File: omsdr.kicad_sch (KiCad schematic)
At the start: 54 parts, among them J1 I/Q Out, J2 ANT, J3 ISP, J4 LO, J5 I/Q Out, J8 PWR, SW1 SW_SPST, SW2 SW_SPST, T1 CX2074NL, U1 LT6231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

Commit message: Adding year 2022 to copyright info
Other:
- note added: "Design by Matt Weyland (HB9FRV) Based on work by Tony Parks (c) 2017,18,19,22 CC-BY-SA"
- note removed: "Design by Matt Weyland (HB9FRV) Based on work by Tony Parks (c) 2017,18,19, CC-BY-SA"
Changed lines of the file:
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@@
     (effects (font (size 5.0038 5.0038) (thickness 1.0008) bold) (justify left bottom))
   )
-  (text "Design by Matt Weyland (HB9FRV)\n\nBased on work by Tony Parks\n(c) 2017,18,19, CC-BY-SA"
+  (text "Design by Matt Weyland (HB9FRV)\n\nBased on work by Tony Parks\n(c) 2017,18,19,22 CC-BY-SA"
     (at 204.47 158.75 0)
     (effects (font (size 2.9972 2.9972)) (justify left bottom))

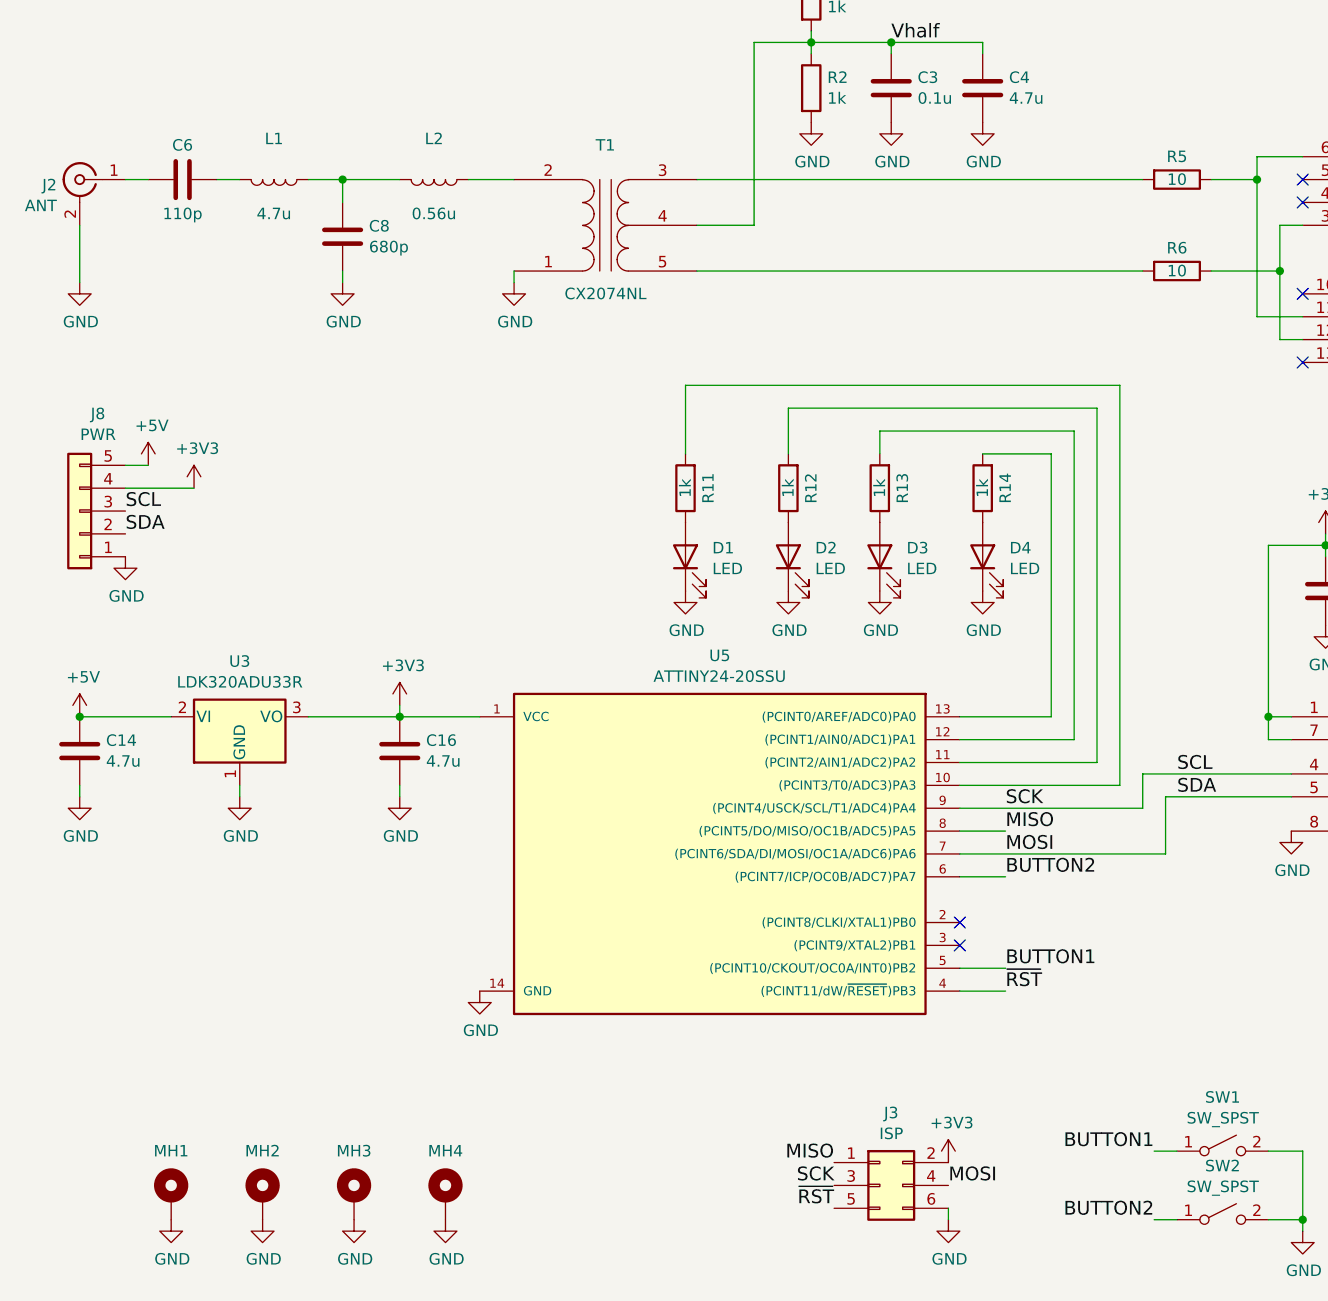
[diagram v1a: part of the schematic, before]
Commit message: Using attiny24 from the KiCad library (sch & pcb)
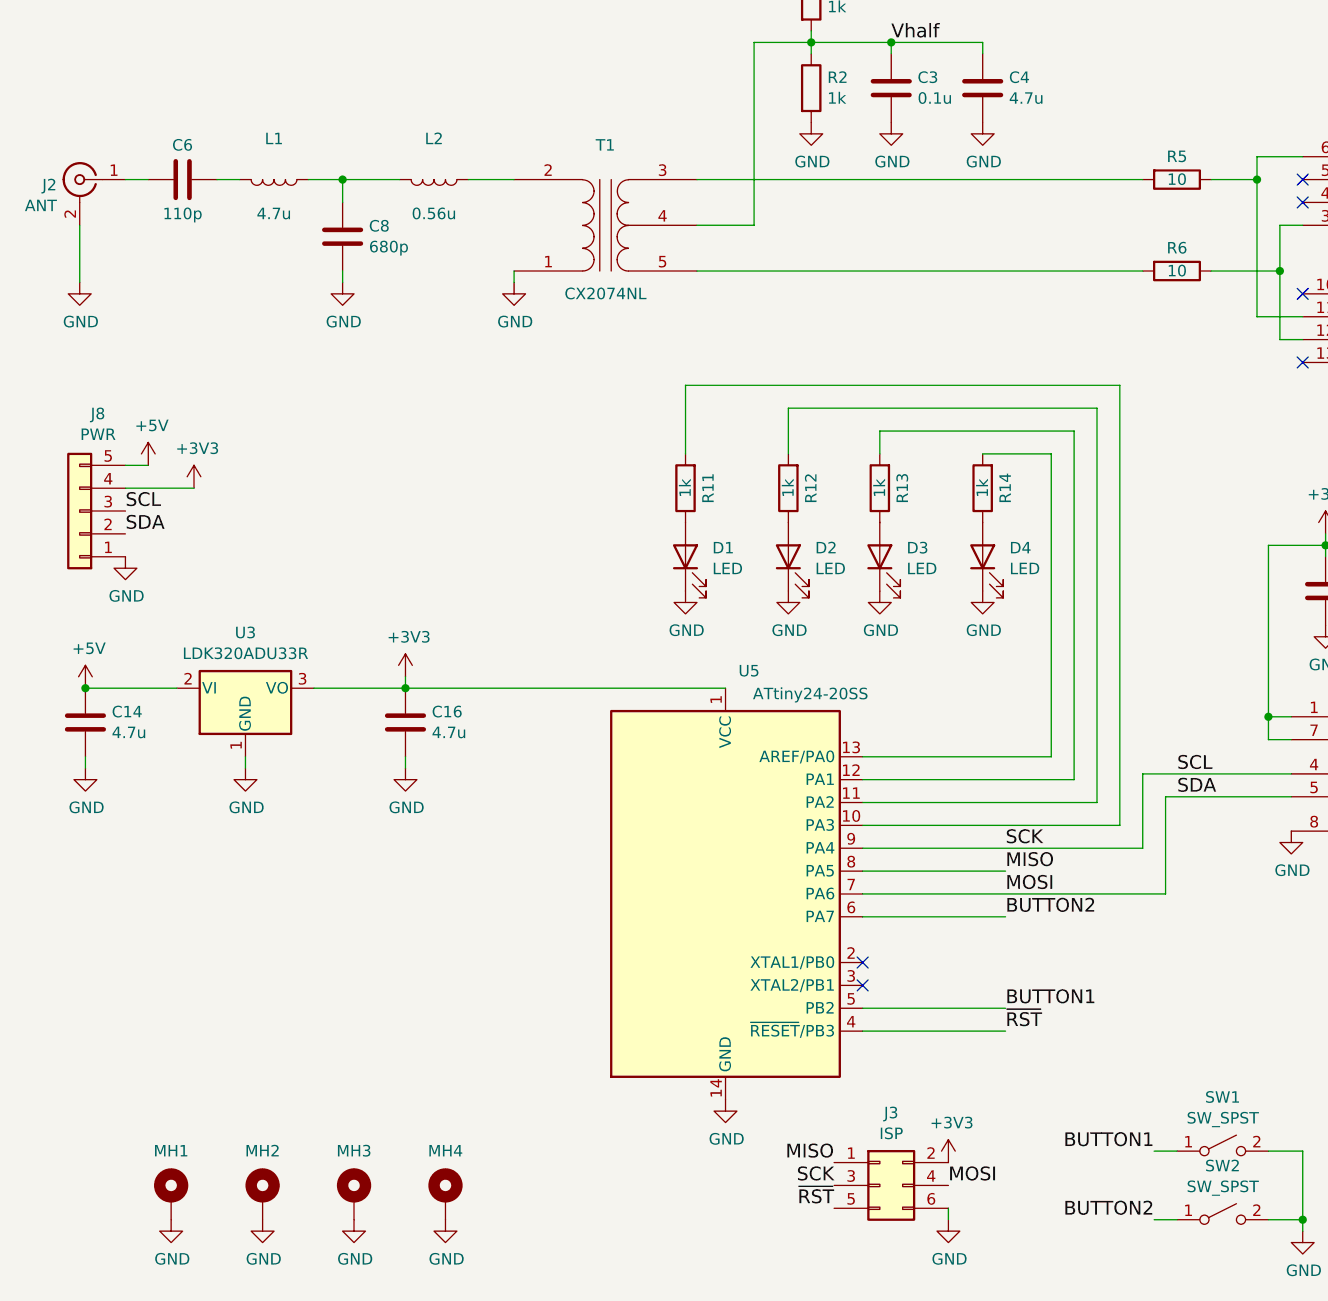
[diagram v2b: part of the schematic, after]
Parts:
- removed U5: ATTINY24-20SSU, IPC7351-Most:SOIC127P600X175-14, symbol omsdr-rescue:ATTINY24-20SSU-atmel
- added U5: ATtiny24-20SS, Package_SO:SOIC-14_3.9x8.7mm_P1.27mm, symbol MCU_Microchip_ATtiny:ATtiny24-20SS
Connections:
- net +3V3: now also U5.1 (VCC)
- net BUTTON1: now also U5.5 (PB2)
- net BUTTON2: now also U5.6 (PA7)
- net GND: now also U5.14 (GND)
- net MISO: now also U5.8 (PA5)
- net MOSI: now also U5.7 (PA6)
- net SCK: now also U5.9 (PA4)
- net ~{RST}: now also U5.4 (~{RESET}/PB3)
- net at R11.2: now also U5.10 (PA3)
- net at R12.2: now also U5.11 (PA2)
- net at R13.2: now also U5.12 (PA1)
- net at R14.2: now also U5.13 (AREF/PA0)
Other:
- moved on the sheet: C14, C16, U3

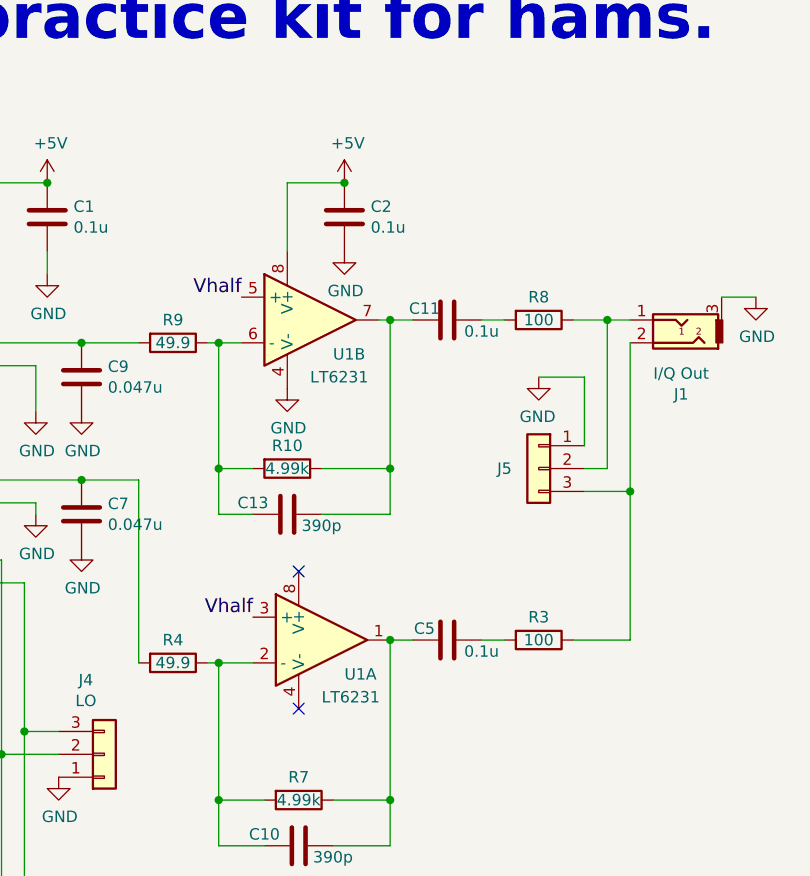
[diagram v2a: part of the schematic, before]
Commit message: Using LC6231 from the KiCad library (sch & pcb)
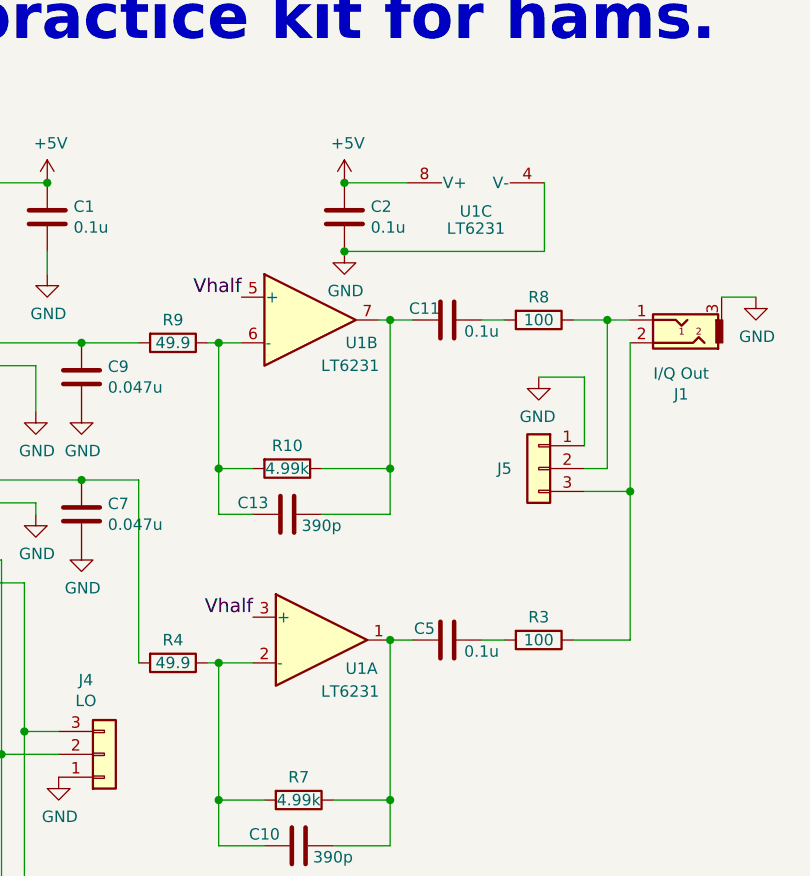
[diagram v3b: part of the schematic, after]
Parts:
- removed U1: LT6231, IPC7351-Most:SOIC127P600X175-8, symbol omsdr-rescue:LT6233-linear
- added U1: LT6231, Package_SO:SO-8_3.9x4.9mm_P1.27mm, symbol Amplifier_Operational:LT6234
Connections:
- net +5V: now also U1.8 (V+)
- net GND: now also U1.4 (V-)
- net Vhalf: now also U1.3 (+), U1.5 (+)
- net at C10.2, C5.1, R7.1: now also U1.1
- net at C10.1, R4.1, R7.2: now also U1.2 (-)
- net at C13.1, R10.2, R9.1: now also U1.6 (-)
- net at C11.1, C13.2, R10.1: now also U1.7
- no-connect marks 9 -> 7

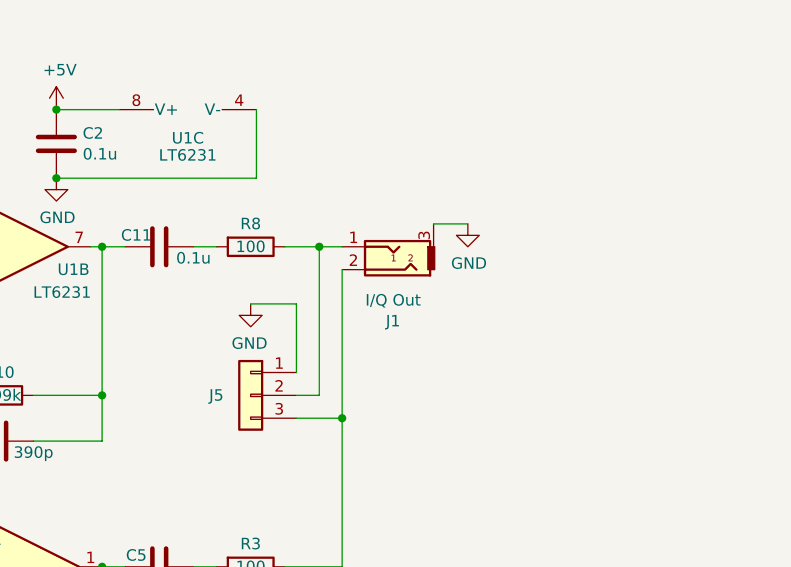
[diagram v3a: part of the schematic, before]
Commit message: Using headphone connector from the KiCad library (sch & pcb)
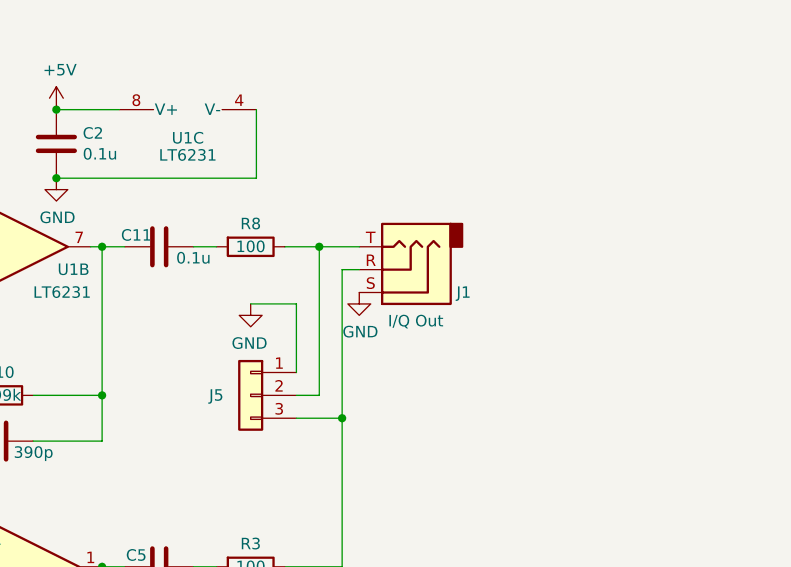
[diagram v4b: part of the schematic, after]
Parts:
- removed J1: I/Q Out, conn-cui:CONN-SJ-3523-SMT, symbol omsdr-rescue:Audio-Jack-3-Connector
- added J1: I/Q Out, Connector_Audio:Jack_3.5mm_CUI_SJ-3523-SMT_Horizontal, symbol Connector:AudioJack3
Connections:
- net GND: now also J1.S
- net at J5.2 (Pin_2), R8.1: now also J1.T
- net at J5.3 (Pin_3), R3.1: now also J1.R
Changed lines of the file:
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@@
     (stroke (width 0) (type default) (color 0 0 0 0))
   )
-  (wire (pts (xy 261.62 57.15) (xy 264.16 57.15))
+  (wire (pts (xy 261.62 57.15) (xy 266.065 57.15))
     (stroke (width 0) (type default) (color 0 0 0 0))
   )
@@
     (stroke (width 0) (type default) (color 0 0 0 0))
   )
-  (wire (pts (xy 274.32 54.61) (xy 278.13 54.61))
-    (stroke (width 0) (type default) (color 0 0 0 0))
-  )
   (wire (pts (xy 157.48 170.18) (xy 161.29 170.18))
     (stroke (width 0) (type default) (color 0 0 0 0))
@@
   )
   (wire (pts (xy 222.25 73.66) (xy 218.44 73.66))
+    (stroke (width 0) (type default) (color 0 0 0 0))
+  )
+  (wire (pts (xy 264.16 59.69) (xy 266.065 59.69))
     (stroke (width 0) (type default) (color 0 0 0 0))
   )
@@
     (pin "2")
   )
-  (symbol (lib_id "omsdr-rescue:Audio-Jack-3-Connector") (at 269.24 57.15 180) (unit 1)
-    (in_bom yes) (on_board yes)
-    (property "Reference" "J1" (id 0) (at 269.8242 65.405 0))
-    (property "Value" "I/Q Out" (id 1) (at 269.8242 63.0936 0))
-    (property "Footprint" "conn-cui:CONN-SJ-3523-SMT" (id 2) (at 262.89 59.69 0)
-      (effects (font (size 1.27 1.27)) hide)
-    )
-    (property "Datasheet" "" (id 3) (at 262.89 59.69 0)
-      (effects (font (size 1.27 1.27)) hide)
-    )
-    (property "BOM" "DIST DIGIKEY CP-3523SJCT-ND" (id 4) (at 269.24 57.15 0)
-      (effects (font (size 1.524 1.524)) hide)
-    )
-    (pin "1")
-    (pin "2")
-    (pin "3")
-  )
-  (symbol (lib_id "power:GND") (at 278.13 54.61 0) (unit 1)
-    (in_bom yes) (on_board yes)
-    (property "Reference" "#PWR016" (id 0) (at 278.13 60.96 0)
-      (effects (font (size 1.27 1.27)) hide)
-    )
-    (property "Value" "GND" (id 1) (at 278.257 59.0042 0))
-    (property "Footprint" "" (id 2) (at 278.13 54.61 0)
-      (effects (font (size 1.27 1.27)) hide)
-    )
-    (property "Datasheet" "" (id 3) (at 278.13 54.61 0)
+  (symbol (lib_id "power:GND") (at 266.065 62.23 0) (unit 1)
+    (in_bom yes) (on_board yes)
+    (property "Reference" "#PWR016" (id 0) (at 266.065 68.58 0)
+      (effects (font (size 1.27 1.27)) hide)
+    )
+    (property "Value" "GND" (id 1) (at 266.192 66.6242 0))
+    (property "Footprint" "" (id 2) (at 266.065 62.23 0)
+      (effects (font (size 1.27 1.27)) hide)
+    )
+    (property "Datasheet" "" (id 3) (at 266.065 62.23 0)
       (effects (font (size 1.27 1.27)) hide)
     )
@@
     (pin "9")
   )
+  (symbol (lib_id "Connector:AudioJack3") (at 271.145 59.69 180) (unit 1)
+    (in_bom yes) (on_board yes)
+    (property "Reference" "J1" (id 0) (at 276.86 62.23 0)
+      (effects (font (size 1.27 1.27)) (justify right))
+    )
+    (property "Value" "I/Q Out" (id 1) (at 269.24 65.405 0)
+      (effects (font (size 1.27 1.27)) (justify right))
+    )
+    (property "Footprint" "Connector_Audio:Jack_3.5mm_CUI_SJ-3523-SMT_Horizontal" (id 2) (at 271.145 59.69 0)
+      (effects (font (size 1.27 1.27)) hide)
+    )
+    (property "Datasheet" "~" (id 3) (at 271.145 59.69 0)
+      (effects (font (size 1.27 1.27)) hide)
+    )
+    (property "BOM" "DIST DIGIKEY CP-3523SJCT-ND" (id 4) (at 271.145 59.69 0)
+      (effects (font (size 1.524 1.524)) hide)
+    )
+    (pin "R")
+    (pin "S")
+    (pin "T")
+  )
   (sheet_instances
     (path "/" (page "1"))
@@
       (reference "D4") (unit 1) (value "LED") (footprint "LED_SMD:LED_0805_2012Metric_Pad1.15x1.40mm_HandSolder")
     )
-    (path "/00000000-0000-0000-0000-00005a050db8"
-      (reference "J1") (unit 1) (value "I/Q Out") (footprint "conn-cui:CONN-SJ-3523-SMT")
+    (path "/ecbf5afe-613b-432f-a930-892c9ca3cd88"
+      (reference "J1") (unit 1) (value "I/Q Out") (footprint "Connector_Audio:Jack_3.5mm_CUI_SJ-3523-SMT_Horizontal")
     )
     (path "/00000000-0000-0000-0000-00005a049e90"
